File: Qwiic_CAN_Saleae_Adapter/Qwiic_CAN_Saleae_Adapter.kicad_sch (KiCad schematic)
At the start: 13 parts, among them J1 Screw_Terminal_01x03, J3 Saleae, J4 Conn_QWIIC_Horizontal, U1 MAX33040

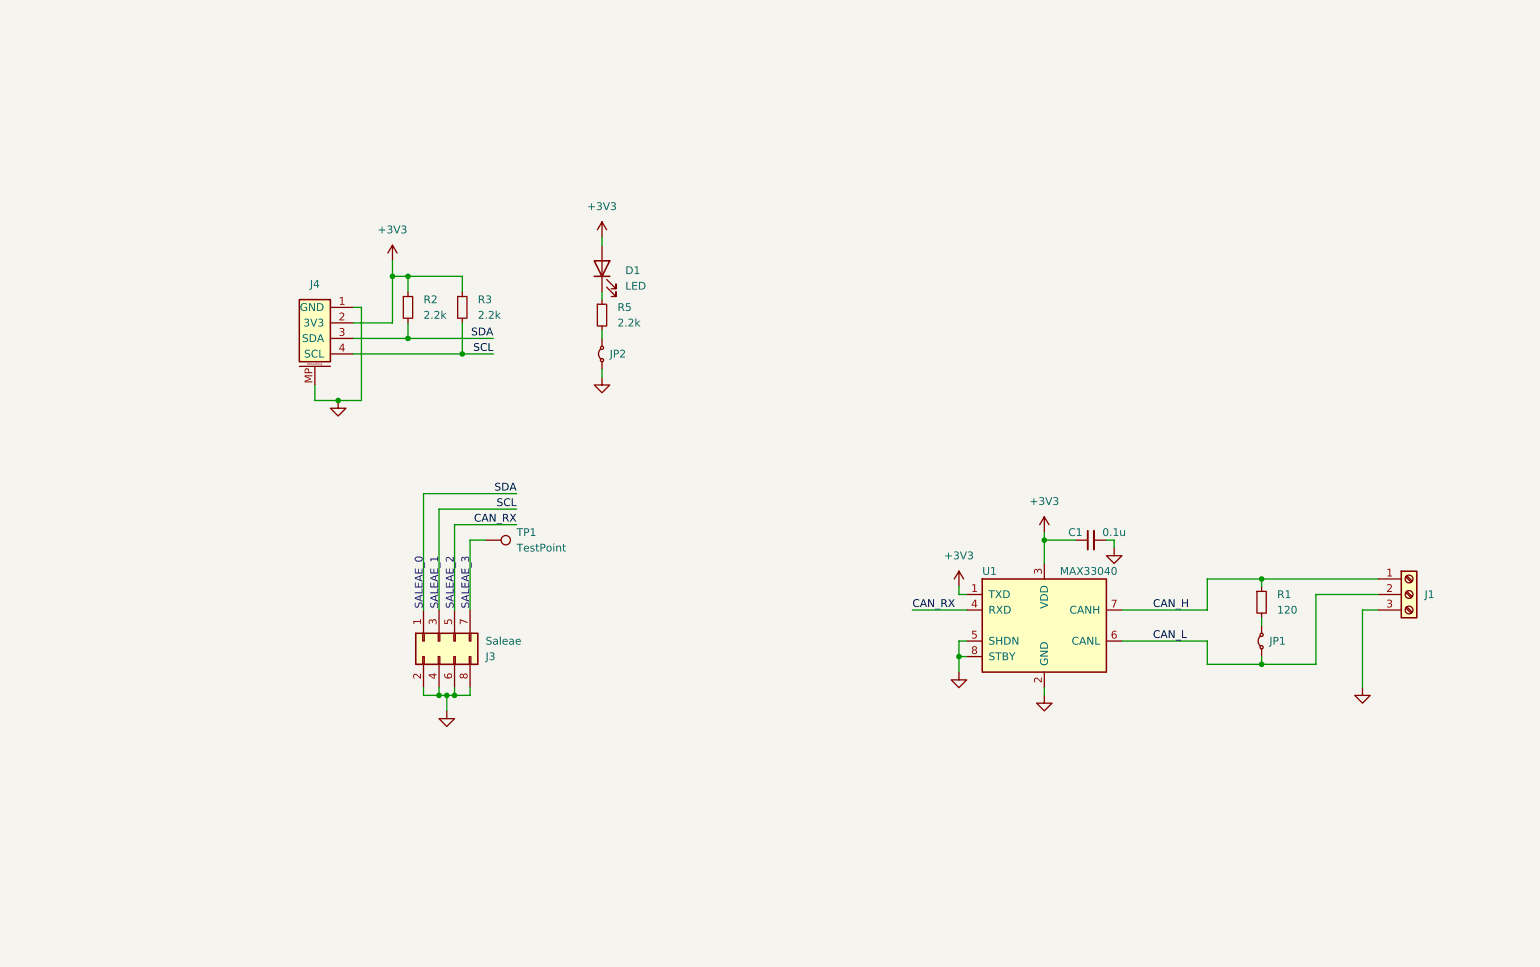
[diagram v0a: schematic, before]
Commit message: V2 QWIIC board
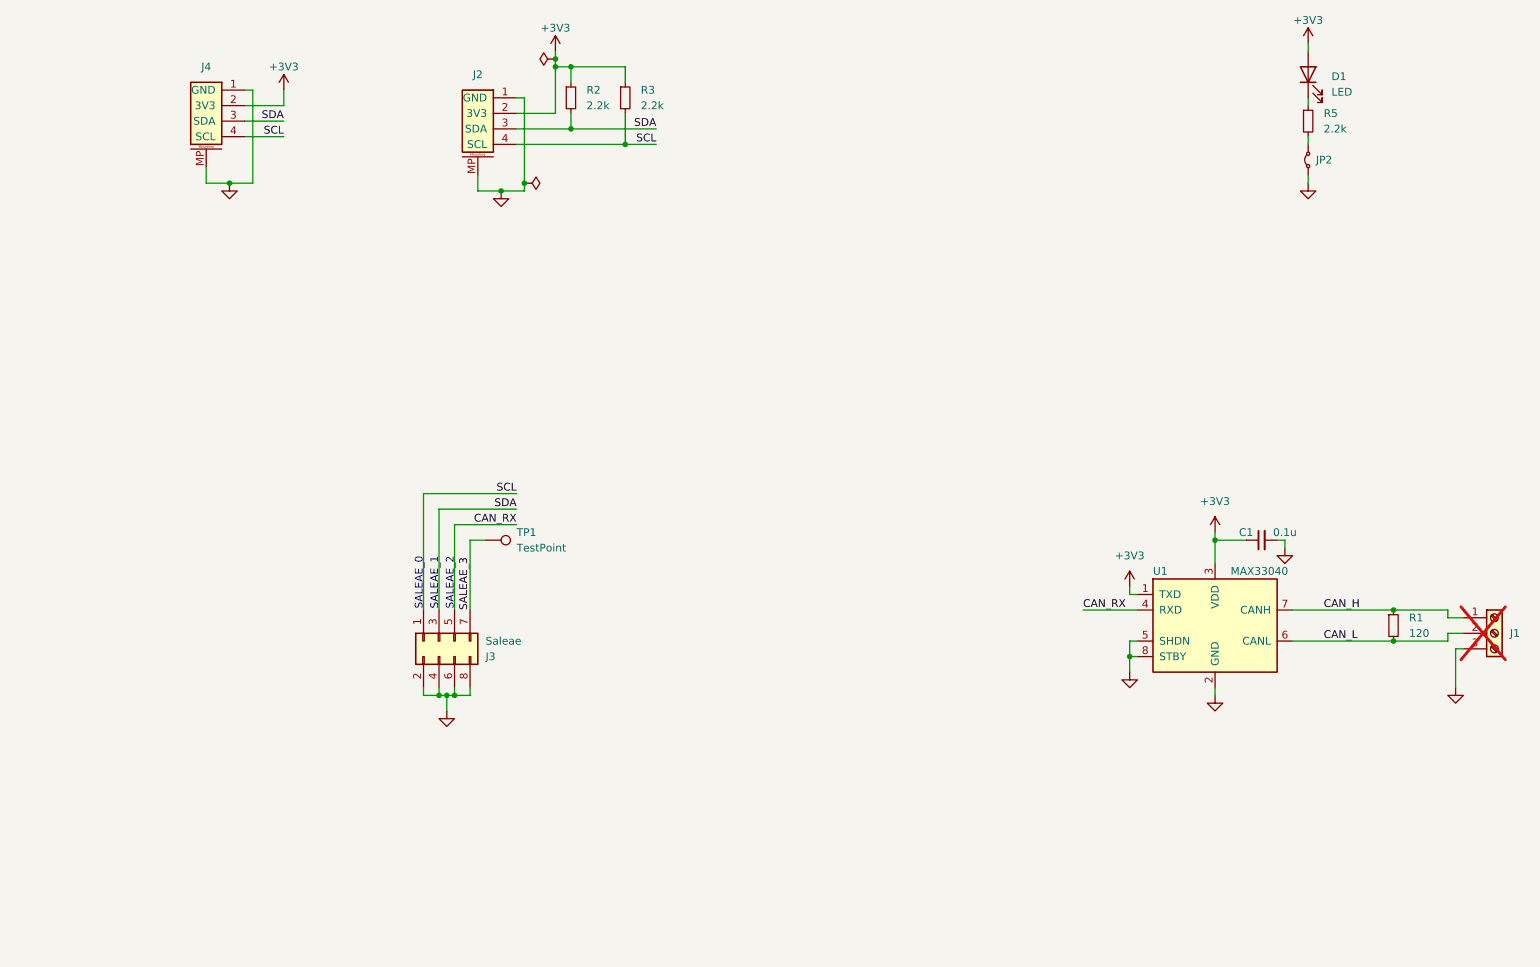
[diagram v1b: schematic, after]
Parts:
- removed J4: Conn_QWIIC_Horizontal, Connector_JST:JST_SH_SM04B-SRSS-TB_1x04-1MP_P1.00mm_Horizontal, symbol SKEC_Symbols:Conn_QWIIC_Horizontal
- removed JP1: Jumper_2_Small_Bridged, Jumper:SolderJumper-2_P1.3mm_Bridged_RoundedPad1.0x1.5mm, symbol Jumper:Jumper_2_Small_Bridged
- added J2, J4: Conn_QWIIC_Vertical, Connector_JST:JST_SH_BM04B-SRSS-TB_1x04-1MP_P1.00mm_Vertical, symbol SKEC_Symbols:Conn_QWIIC_Vertical
- J1: footprint TerminalBlock_4Ucon:TerminalBlock_4Ucon_1x03_P3.50mm_Horizontal -> SKEC_Footprints:Screw_Terminal_01x03_BoardEdge_Horizontal; MPN (none) -> C466971; now not fitted; now left out of the parts list
- R1: footprint Resistor_SMD:R_0402_1005Metric_Pad0.72x0.64mm_HandSolder -> Resistor_SMD:R_0603_1608Metric_Pad0.98x0.95mm_HandSolder
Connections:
- net +3V3: now also J2.2 (3V3), J4.2 (3V3)
- net CAN_L: now also R1.2
- net GND: now also J2.1 (GND), J2.MP, J4.1 (GND), J4.MP
- net SCL: now also J3.1 (Pin_1), J2.4 (SCL), J4.4 (SCL); no longer J3.3 (Pin_3)
- net SDA: now also J3.3 (Pin_3), J2.3 (SDA), J4.3 (SDA); no longer J3.1 (Pin_1)
- net SALEAE_3: now reaches J3.7 (Pin_7), TP1.1
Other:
- note removed: "SALEAE_3"
- moved on the sheet: C1, D1, JP2, R1, R2, R3, R5, U1

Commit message: Capture Ideas post v2 and including GDS mount
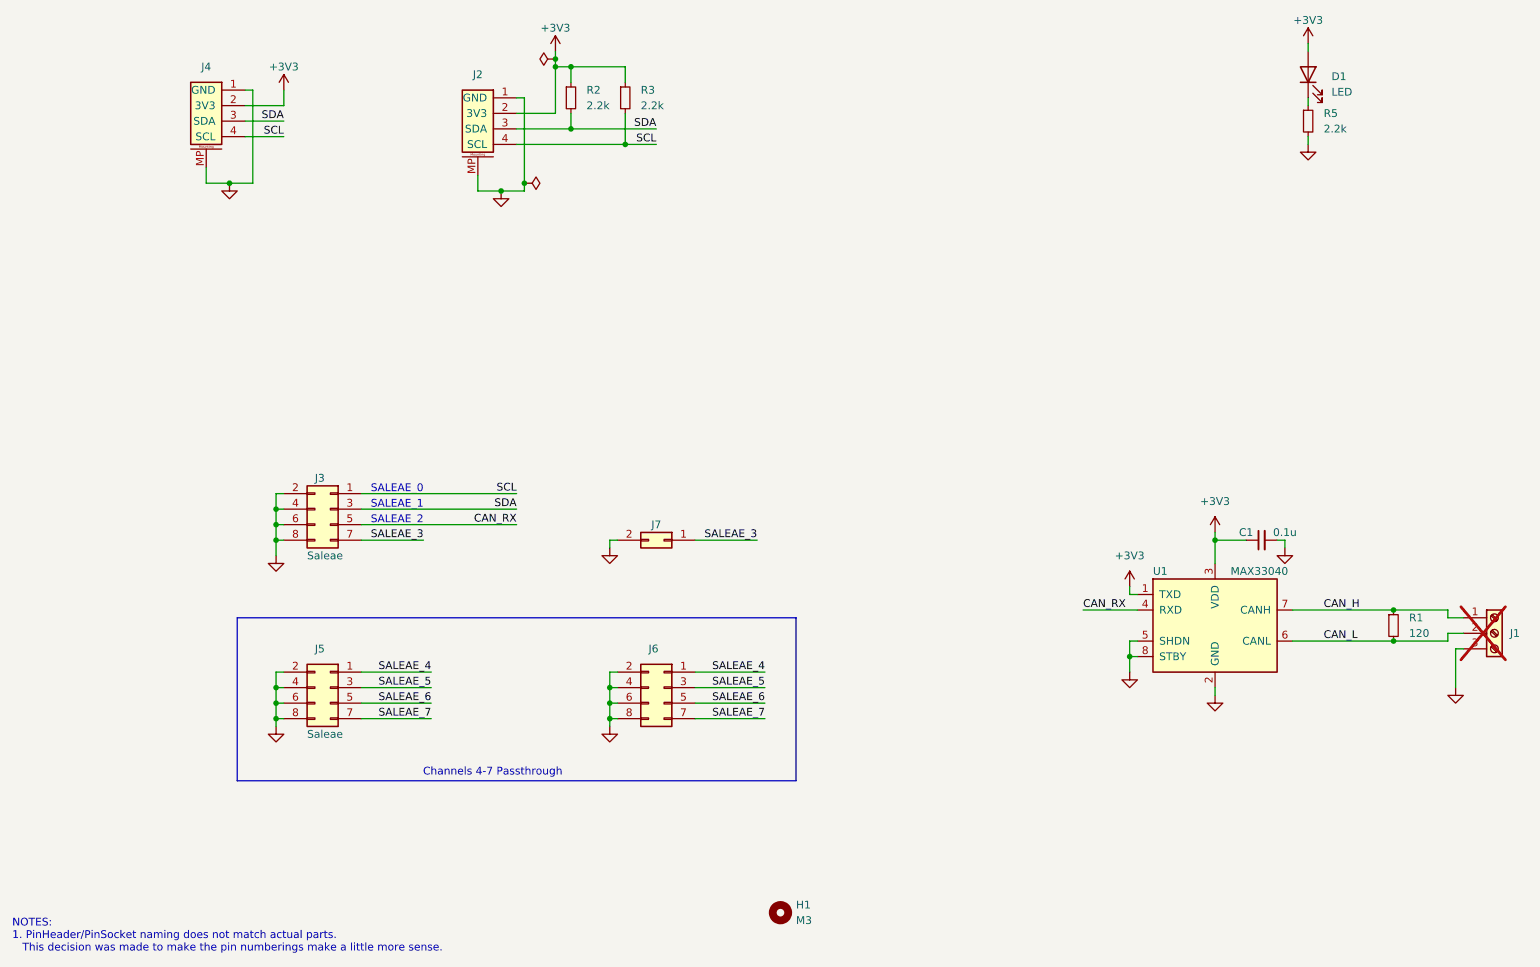
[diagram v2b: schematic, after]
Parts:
- removed JP2: Jumper_2_Small_Bridged, Jumper:SolderJumper-2_P1.3mm_Bridged_RoundedPad1.0x1.5mm, symbol Jumper:Jumper_2_Small_Bridged
- removed TP1: TestPoint, Connector_PinHeader_2.54mm:PinHeader_1x01_P2.54mm_Vertical, symbol Connector:TestPoint
- added H1: M3, MountingHole:MountingHole_3.2mm_M3_DIN965, symbol Mechanical:MountingHole
- added J5: Saleae, Connector_PinHeader_2.54mm:PinHeader_2x04_P2.54mm_Horizontal, symbol Connector_Generic:Conn_02x04_Odd_Even
- added J6: Saleae, Connector_PinSocket_2.54mm:PinSocket_2x04_P2.54mm_Vertical, symbol Connector_Generic:Conn_02x04_Odd_Even
- added J7: Conn_02x01, Connector_PinSocket_2.54mm:PinSocket_2x01_P2.54mm_Vertical, symbol Connector_Generic:Conn_02x01
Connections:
- net GND: now also R5.2, J5.2 (Pin_2), J5.4 (Pin_4), J5.6 (Pin_6), J5.8 (Pin_8), J6.2 (Pin_2), J6.4 (Pin_4), J6.6 (Pin_6), J6.8 (Pin_8), J7.2 (Pin_2)
- net SALEAE_3: now also J7.1 (Pin_1)
- new net SALEAE_4: J5.1 (Pin_1), J6.1 (Pin_1)
- new net SALEAE_5: J5.3 (Pin_3), J6.3 (Pin_3)
- new net SALEAE_6: J5.5 (Pin_5), J6.5 (Pin_5)
- new net SALEAE_7: J5.7 (Pin_7), J6.7 (Pin_7)
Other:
- note added: "Channels 4-7 Passthrough"
- note added: "NOTES: 1. PinHeader/PinSocket naming does not match actual parts. This decision was made to make the pin numberings make a little more sense."
- moved on the sheet: J3

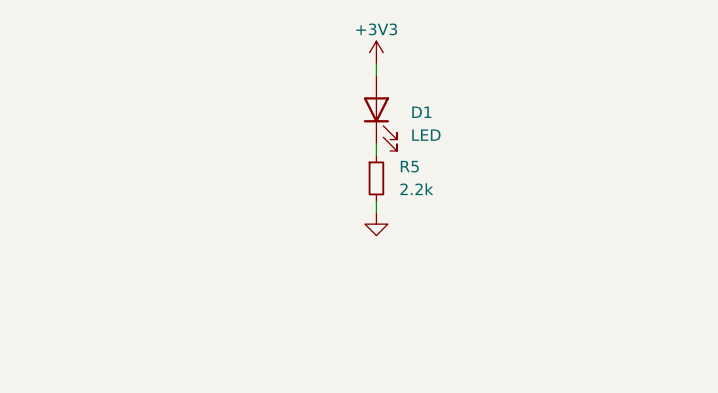
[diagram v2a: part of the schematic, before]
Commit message: V3 of Saleae Adapter
Added the other 4 channels and a mounting hole for the Gridfinity holder
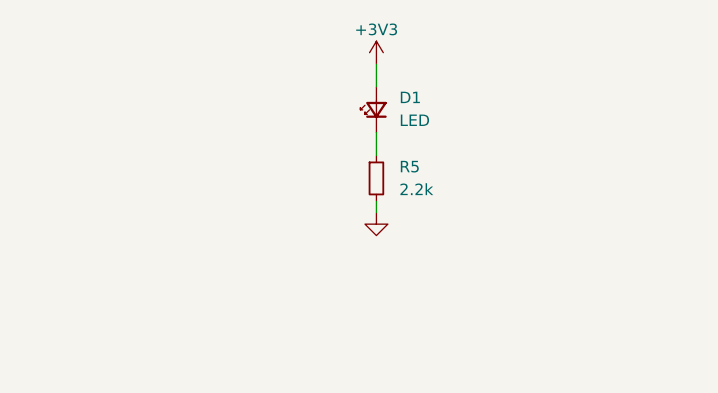
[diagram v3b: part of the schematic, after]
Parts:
- C1: JLCPCB Part No. (none) -> C131394; MPN (none) -> CC0402KRX7R9BB104
- D1: symbol Device:LED -> PartsBox:LTST-C190KRKT; JLCPCB Part No. (none) -> C94869; MPN (none) -> LTST-C190KRKT; Manufacturer (none) -> Lite-On; PartsBox ID (none) -> b7k17z15cekaq9nt767vczf2qm; Type (none) -> Linked
- J2, J4: symbol SKEC_Symbols:Conn_QWIIC_Vertical -> PartsBox:BM04B-SRSS-TBT(LF)(SN); FT Position Offset (none) -> 0,-0.381; FT Rotation Offset (none) -> 180; JLCPCB Part No. (none) -> C495539; MPN C495539 -> BM04B-SRSS-TBT(LF)(SN); Manufacturer (none) -> JST; PartsBox ID (none) -> 4nga0y2dyjgrba8226q50sap03; Type (none) -> Linked
- J3, J5: FT Rotation Offset (none) -> 90; JLCPCB Part No. (none) -> C2897424; MPN C7529541 -> (none)
- J6: FT Rotation Offset (none) -> 90; JLCPCB Part No. (none) -> C7501275; MPN C7529541 -> (none)
- J7: JLCPCB Part No. (none) -> C492401
- R1: JLCPCB Part No. (none) -> C114640; MPN (none) -> RC0603FR-07120RL
- R2, R3, R5: JLCPCB Part No. (none) -> C114762
- U1: JLCPCB Part No. (none) -> C5221297; MPN C5221297 -> (none)
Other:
- moved on the sheet: D1
